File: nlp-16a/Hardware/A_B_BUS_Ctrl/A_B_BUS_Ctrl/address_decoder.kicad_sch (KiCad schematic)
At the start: 4 parts

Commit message: 微修正
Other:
- note added: "Bankレジスタを削除．代わりにRegFを作成．"
- note added: "RegF"
- note added: "ZeroRegは内部モード時に常に指定される(レジスタとしての実体が無いため問題にならない．入力値が無い場合に確実に0となる)"
- note added: "緑:内部処理で使用されるレジスタ"
- note removed: "Bank(無し)"
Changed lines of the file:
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@@
     (effects (font (size 1.27 1.27)) (justify left bottom))
   )
-  (text "Bank(無し)" (at 156.21 132.08 0)
+  (text "MEM" (at 156.21 132.08 0)
     (effects (font (size 1.27 1.27)) (justify left bottom))
   )
@@
     (effects (font (size 1.27 1.27)) (justify left bottom))
   )
-  (text "MEM" (at 133.35 132.08 0)
+  (text "RegF" (at 133.35 132.08 0)
     (effects (font (size 1.27 1.27)) (justify left bottom))
   )
@@
     (effects (font (size 1.27 1.27)) (justify left bottom))
   )
+  (text "緑:内部処理で使用されるレジスタ" (at 82.55 38.1 0)
+    (effects (font (size 1.27 1.27)) (justify left bottom))
+  )
   (text "RegA" (at 201.93 66.04 0)
+    (effects (font (size 1.27 1.27)) (justify left bottom))
+  )
+  (text "ZeroRegは内部モード時に常に指定される(レジスタとしての実体が無いため問題にならない．入力値が無い場合に確実に0となる)"
+    (at 185.42 165.1 0)
+    (effects (font (size 1.27 1.27)) (justify left bottom))
+  )
+  (text "Bankレジスタを削除．代わりにRegFを作成．" (at 129.54 165.1 0)
     (effects (font (size 1.27 1.27)) (justify left bottom))
   )
@@
     (effects (font (size 1.27 1.27)) (justify right))
   )
-  (hierarchical_label "~Bank" (shape input) (at 167.64 161.29 180)
-    (effects (font (size 1.27 1.27)) (justify right))
-  )
   (hierarchical_label "~IR3" (shape input) (at 144.78 95.25 180)
     (effects (font (size 1.27 1.27)) (justify right))
@@
     (effects (font (size 1.27 1.27)) (justify right))
   )
-  (hierarchical_label "~MEM" (shape input) (at 144.78 161.29 180)
+  (hierarchical_label "~MEM" (shape input) (at 167.64 161.29 180)
     (effects (font (size 1.27 1.27)) (justify right))
   )
@@
     (pin "1")
   )
+  (symbol (lib_id "power:VDD") (at 144.78 161.29 0) (unit 1)
+    (in_bom yes) (on_board yes)
+    (property "Reference" "#PWR?" (id 0) (at 144.78 165.1 0)
+      (effects (font (size 1.27 1.27)) hide)
+    )
+    (property "Value" "VDD" (id 1) (at 140.97 160.02 0))
+    (property "Footprint" "" (id 2) (at 144.78 161.29 0)
+      (effects (font (size 1.27 1.27)) hide)
+    )
+    (property "Datasheet" "" (id 3) (at 144.78 161.29 0)
+      (effects (font (size 1.27 1.27)) hide)
+    )
+    (pin "1")
+  )
   (symbol (lib_id "power:VDD") (at 236.22 95.25 0) (unit 1)
     (in_bom yes) (on_board yes)
@@
   (sheet (at 175.26 59.69) (size 19.05 11.43)
     (stroke (width 0.1524) (type solid) (color 0 0 0 0))
-    (fill (color 0 0 0 0.0000))
+    (fill (color 111 255 1 1.0000))
     (property "Sheet name" "decoder4" (id 0) (at 181.61 62.23 0)
       (effects (font (size 1.27 1.27)) (justify left bottom))
@@
   (sheet (at 243.84 125.73) (size 19.05 11.43)
     (stroke (width 0.1524) (type solid) (color 0 0 0 0))
-    (fill (color 0 0 0 0.0000))
+    (fill (color 111 255 1 1.0000))
     (property "Sheet name" "decoder15" (id 0) (at 250.19 128.27 0)
       (effects (font (size 1.27 1.27)) (justify left bottom))
@@
   (sheet (at 106.68 59.69) (size 19.05 11.43)
     (stroke (width 0.1524) (type solid) (color 0 0 0 0))
-    (fill (color 0 0 0 0.0000))
+    (fill (color 111 255 1 1.0000))
     (property "Sheet name" "decoder1" (id 0) (at 113.03 62.23 0)
       (effects (font (size 1.27 1.27)) (justify left bottom))
@@
   (sheet (at 220.98 125.73) (size 19.05 11.43)
     (stroke (width 0.1524) (type solid) (color 0 0 0 0))
-    (fill (color 0 0 0 0.0000))
+    (fill (color 111 255 1 1.0000))
     (property "Sheet name" "decoder14" (id 0) (at 227.33 128.27 0)
       (effects (font (size 1.27 1.27)) (justify left bottom))
@@
   (sheet (at 175.26 125.73) (size 19.05 11.43)
     (stroke (width 0.1524) (type solid) (color 0 0 0 0))
-    (fill (color 0 0 0 0.0000))
+    (fill (color 111 255 1 1.0000))
     (property "Sheet name" "decoder12" (id 0) (at 181.61 128.27 0)
       (effects (font (size 1.27 1.27)) (justify left bottom))
@@
   (sheet (at 198.12 125.73) (size 19.05 11.43)
     (stroke (width 0.1524) (type solid) (color 0 0 0 0))
-    (fill (color 0 0 0 0.0000))
+    (fill (color 111 255 1 1.0000))
     (property "Sheet name" "decoder13" (id 0) (at 204.47 128.27 0)
       (effects (font (size 1.27 1.27)) (justify left bottom))
@@
   (sheet (at 152.4 59.69) (size 19.05 11.43)
     (stroke (width 0.1524) (type solid) (color 0 0 0 0))
-    (fill (color 0 0 0 0.0000))
+    (fill (color 111 255 1 1.0000))
     (property "Sheet name" "decoder3" (id 0) (at 158.75 62.23 0)
       (effects (font (size 1.27 1.27)) (justify left bottom))
@@
   (sheet (at 152.4 125.73) (size 19.05 11.43)
     (stroke (width 0.1524) (type solid) (color 0 0 0 0))
-    (fill (color 0 0 0 0.0000))
+    (fill (color 111 255 1 1.0000))
     (property "Sheet name" "decoder11" (id 0) (at 158.75 128.27 0)
       (effects (font (size 1.27 1.27)) (justify left bottom))
@@
   (sheet (at 129.54 59.69) (size 19.05 11.43)
     (stroke (width 0.1524) (type solid) (color 0 0 0 0))
-    (fill (color 0 0 0 0.0000))
+    (fill (color 111 255 1 1.0000))
     (property "Sheet name" "decoder2" (id 0) (at 135.89 62.23 0)
       (effects (font (size 1.27 1.27)) (justify left bottom))
@@
   (sheet (at 83.82 59.69) (size 19.05 11.43)
     (stroke (width 0.1524) (type solid) (color 0 0 0 0))
-    (fill (color 0 0 0 0.0000))
+    (fill (color 111 255 1 1.0000))
     (property "Sheet name" "decoder0" (id 0) (at 90.17 62.23 0)
       (effects (font (size 1.27 1.27)) (justify left bottom))

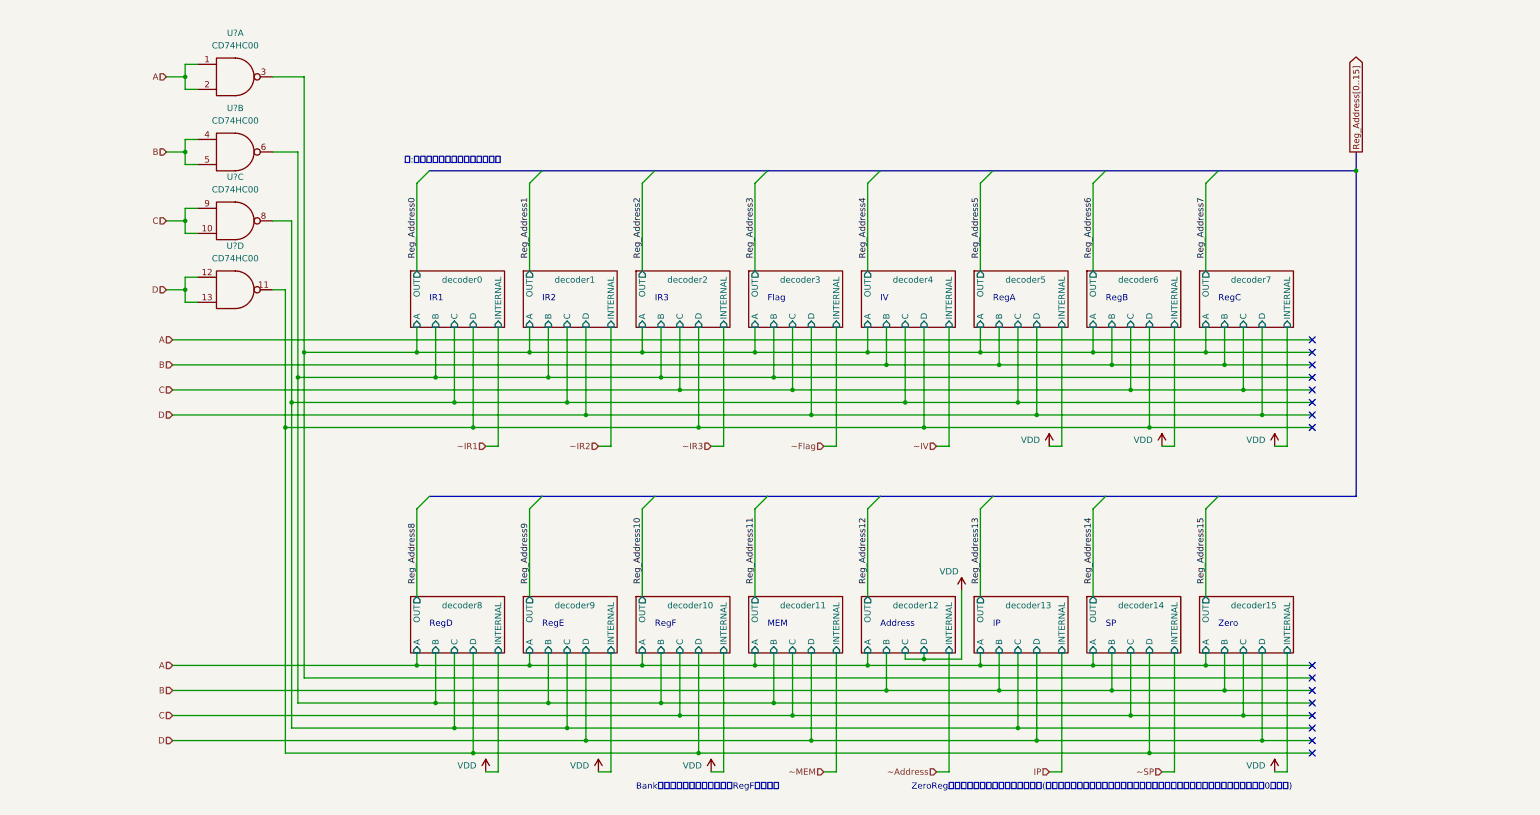
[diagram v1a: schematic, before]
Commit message: 内部処理モードを追加
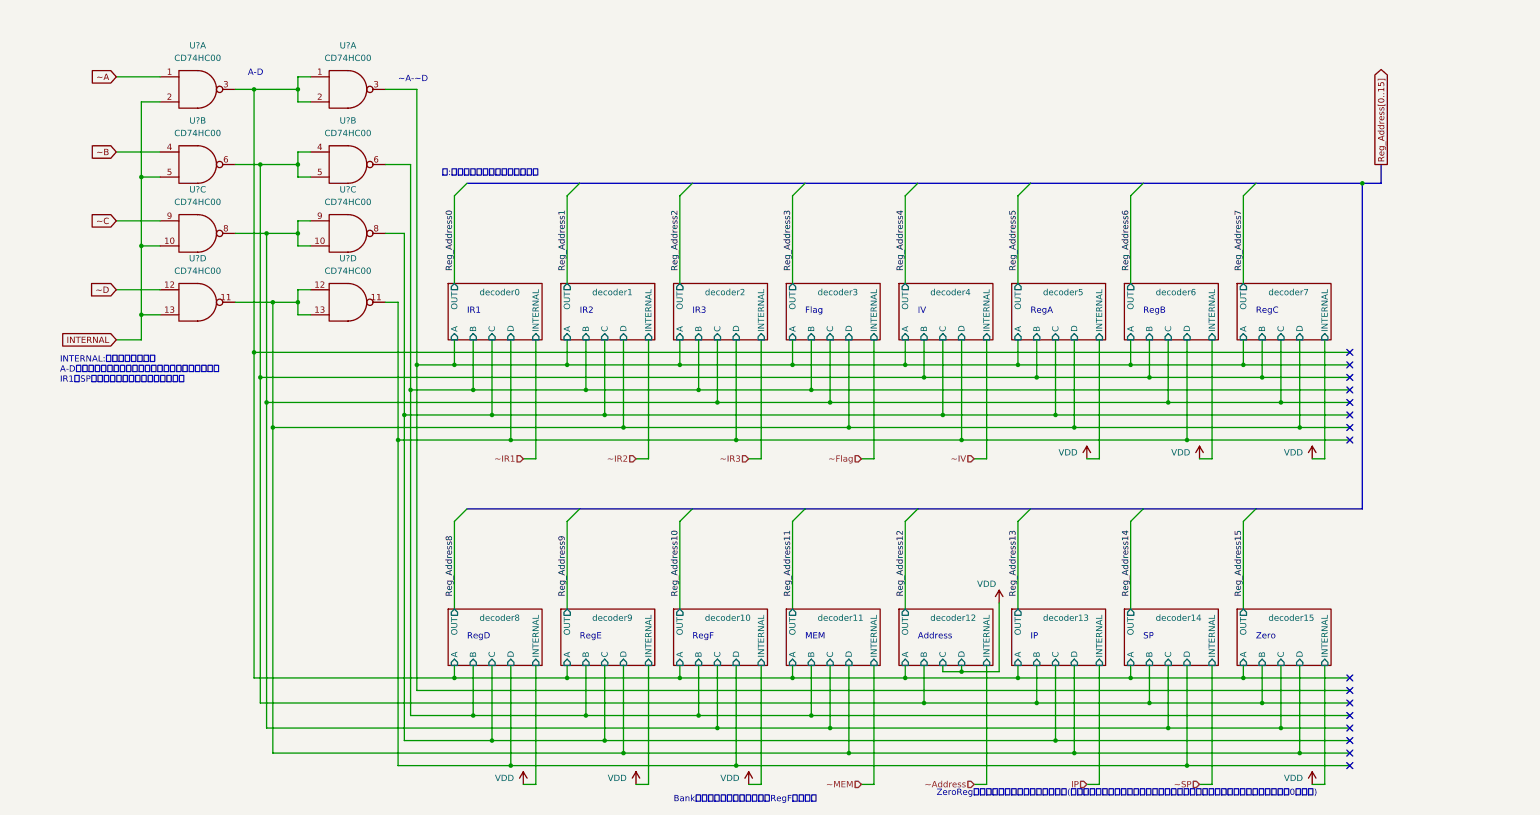
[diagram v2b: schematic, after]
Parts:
- added U? (x4): CD74HC00, symbol CD74HCXX:CD74HC00
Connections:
- net GND: now also U?.7 (GND), U?.7 (GND), U?.7 (GND), U?.7 (GND)
- net VCC: now also U?.14 (VCC), U?.14 (VCC), U?.14 (VCC), U?.14 (VCC)
- net A renamed decoder10/A
- net decoder10/A: now also U?.3
- net B renamed decoder12/B
- net decoder12/B: now also U?.6
- net C renamed decoder10/C
- net decoder10/C: now also U?.8
- net D renamed decoder1/D
- net decoder1/D: now also U?.11
- new net INTERNAL: U?.10, U?.13, U?.2, U?.5
- new net ~A: U?.1
- new net ~B: U?.4
- new net ~C: U?.9
- new net ~D: U?.12
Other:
- note added: "A-D"
- note added: "INTERNAL:内部処理モード． A-Dによって入力されたレジスタアドレスを無視して， IR1～SPによってレジスタを直接指定する"
- note added: "~A-~D"
- moved on the sheet: U?A, U?B, U?C, U?D

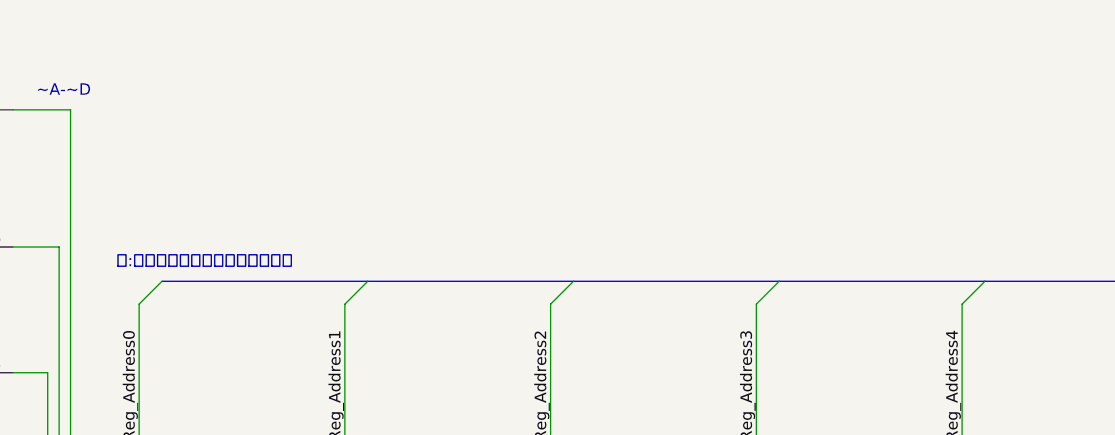
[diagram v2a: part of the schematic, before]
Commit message: 信号補正部追加
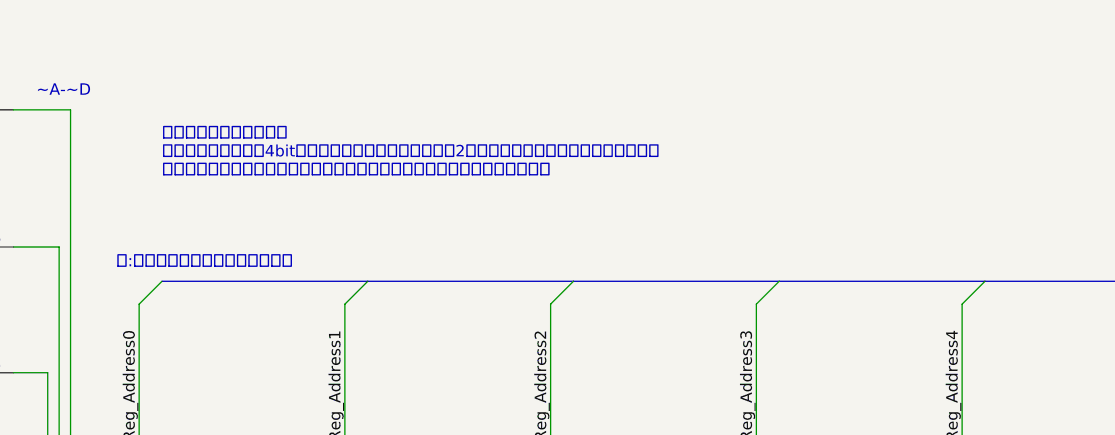
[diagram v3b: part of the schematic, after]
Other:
- note added: "レジスタアドレス変換部 レジスタアドレスは4bitの数値で送られてくるが，その2進数値をデコードし各レジスタに配る また，内部処理でレジスタを使用しやすくするための内部処理モードがある"
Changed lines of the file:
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@@
+    (effects (font (size 1.27 1.27)) (justify left bottom))
+  )
+  (text "レジスタアドレス変換部\nレジスタアドレスは4bitの数値で送られてくるが，その2進数値をデコードし各レジスタに配る\nまた，内部処理でレジスタを使用しやすくするための内部処理モードがある"
+    (at 95.25 30.48 0)
     (effects (font (size 1.27 1.27)) (justify left bottom))
   )

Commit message: 配線作業開始
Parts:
- U41, U42: renamed from U?; footprint (none) -> Package_DIP:DIP-14_W7.62mm
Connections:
- net decoder0/A: now also U41.8; no longer U41.3
- net decoder0/B: now also U41.6; no longer U41.6
- net decoder0/C: now also U42.8; no longer U42.8
- net decoder0/D: now also U42.6; no longer U42.11
- net decoder1/D: now also U42.3, U42.4, U42.5; no longer U42.11, U42.12, U42.13
- net decoder10/A: now also U41.10, U41.11, U41.9; no longer U41.1, U41.2, U41.3
- net decoder10/C: now also U42.10, U42.11, U42.9; no longer U42.10, U42.8, U42.9
- net decoder12/B: now also U41.3, U41.4, U41.5; no longer U41.4, U41.5, U41.6
- removed net INTERNAL: U41.2, U41.5, U42.10, U42.13
- net ~A renamed Reg_Addr2
- net Reg_Addr2: now also U41.13
- removed net ~B: U41.4
- removed net ~C: U42.9
- net ~D renamed Reg_Addr1
- net Reg_Addr1: now also U41.2
- new net Reg_Addr0: U42.1, U42.13
- new net Reg_Addr3: U41.12
- new net ~INTERNAL: U42.2
- no-connect marks 16 -> 0
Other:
- moved on the sheet: U41A, U41B, U41C, U41D, U42A, U42B, U42C, U42D
